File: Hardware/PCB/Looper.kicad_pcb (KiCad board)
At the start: 2 copper layers, 50 x 110.2 mm, 64 parts, among them J1 Out right, J10 Audio from Daisy, connect to 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, J13 Audio to Daisy, connect to J13, J14 Audio from Daisy, connect to 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, J15 Audio input, connect to J18, J16 Audio output, connect to J17, J17 Audio output, connect to J16, J18 Audio input, connect to J15, J2 In left, J3 Trig Loop, J4 Out left, J5 In right, J6 Eurorack_Power, J9 Audio to Daisy, connect to J13, U1 TL074, U2 TL074

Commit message: Version 1.0 of hardware ordered
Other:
- board text added: "Loop v1.0"
- board text added: "Serial"
- board text added: "by Geir & Adam"
- board text added: "https://github.com/GugeNet/Loop"
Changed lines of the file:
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@@
   (gr_rect (start 33.35 -108.5) (end 39.85 -105.3)
+    (stroke (width 0.15) (type solid)) (fill solid) (layer "B.SilkS"))
+  (gr_rect (start 31.775 -77.2) (end 41.025 -72.4)
     (stroke (width 0.15) (type solid)) (fill solid) (layer "B.SilkS"))
   (gr_rect (start 0 -119.7) (end 20 -9.6)
@@
   (gr_rect (start 0 -128.5) (end 20 0)
     (stroke (width 0.15) (type default)) (fill none) (layer "User.1"))
+  (gr_text "by Geir\n& Adam" (at 40 -80.4) (layer "B.SilkS")
+    (effects (font (size 1.5 1.5) (thickness 0.22)) (justify bottom mirror))
+  )
+  (gr_text "Loop\nv1.0" (at 40.2 -85.2) (layer "B.SilkS")
+    (effects (font (size 2 2) (thickness 0.3)) (justify bottom mirror))
+  )
+  (gr_text "https://github.com/GugeNet/Loop" (at 43.2 -119.4 90) (layer "B.SilkS")
+    (effects (font (size 1 1) (thickness 0.15)) (justify left bottom mirror))
+  )
+  (gr_text "Serial" (at 48.2 -73.6) (layer "B.SilkS")
+    (effects (font (size 1.5 1.5) (thickness 0.22)) (justify left bottom mirror))
+  )
   (segment (start 34.9 -95.5) (end 37.00828 -95.5) (width 0.25) (layer "F.Cu") (net 1))
   (segment (start 31.8 -117.58) (end 34.36 -115.02) (width 0.25) (layer "F.Cu") (net 1))
@@
         (xy 30 -120)
         (xy 50 -120)
-        (xy 50 -72.5)
-        (xy 30 -72.5)
+        (xy 50 -71.7)
+        (xy 30 -71.7)
       )
     )
@@
         (xy 30 -120)
         (xy 50 -120)
-        (xy 50 -72.5)
-        (xy 30 -72.5)
+        (xy 50 -71.7)
+        (xy 30 -71.7)
       )
     )

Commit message: Leveller 1.0b
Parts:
- moved J6 3.06 mm to (36.0, -104.4)
- moved FB1 2.48 mm to (37.2, -99.6)
- moved D1 2.45 mm to (37.1, -101.8)
- moved R22 1.88 mm to (41.0, -99.6)
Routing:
- net -12V: track 33.6 -> 30.6 mm
- net Net-(C9-Pad1): track 6.79 -> 8.73 mm
- net Net-(J18-Pin_3): track 19.2 -> 17.4 mm
- net Net-(D4-K): track 15.0 -> 13.1 mm
- net GND: track 489.2 -> 488.4 mm
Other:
- board text added: "Loop v1.0b"
- board text removed: "Loop v1.0"

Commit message: Fixed power diode polarity
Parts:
- moved FB2 16.6 mm to (35.4, -117.6)
- moved D4 11.7 mm to (40.0, -117.6), turned to 180 degrees
- moved C6 3.67 mm to (43.4, -105.3)
- moved FB1 3.35 mm to (35.1, -102.2), turned to 180 degrees
- moved C4 3.07 mm to (43.4, -112.8), turned to -90 degrees
- moved D1 2.16 mm to (36.0, -100.0), turned to 0 degrees
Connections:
- C4 pad 1: Net-(D4-K) -> +12V
- C6 pad 2: Net-(D1-A) -> -12V
- D1 pad 2: Net-(D1-A) -> -12V
- D4 pad 1: Net-(D4-K) -> +12V
- FB1 pad 1: -12V -> Net-(J6-Pin_1)
- FB2 pad 1: +12V -> Net-(J6-Pin_10)
- J6 pad 1: Net-(D1-A) -> Net-(J6-Pin_1)
- J6 pad 10: Net-(D4-K) -> Net-(J6-Pin_10)
- J6 pad 2: Net-(D1-A) -> Net-(J6-Pin_1)
- J6 pad 9: Net-(D4-K) -> Net-(J6-Pin_10)
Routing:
- net +12V: track 97.7 -> 111.9 mm
- net Net-(D4-K): track 13.1 -> 0.00 mm
- net Net-(D1-A): track 10.9 -> 0.00 mm
- net -12V: track 30.6 -> 39.8 mm
- net GND: track 488.4 -> 495.5 mm
- net Net-(J6-Pin_1): track 0.00 -> 4.70 mm
- net Net-(J6-Pin_10): track 0.00 -> 3.63 mm
- net Net-(D4-A): track 1.62 -> 2.12 mm
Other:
- board text added: "Loop v1.0c"
- board text removed: "Loop v1.0b"

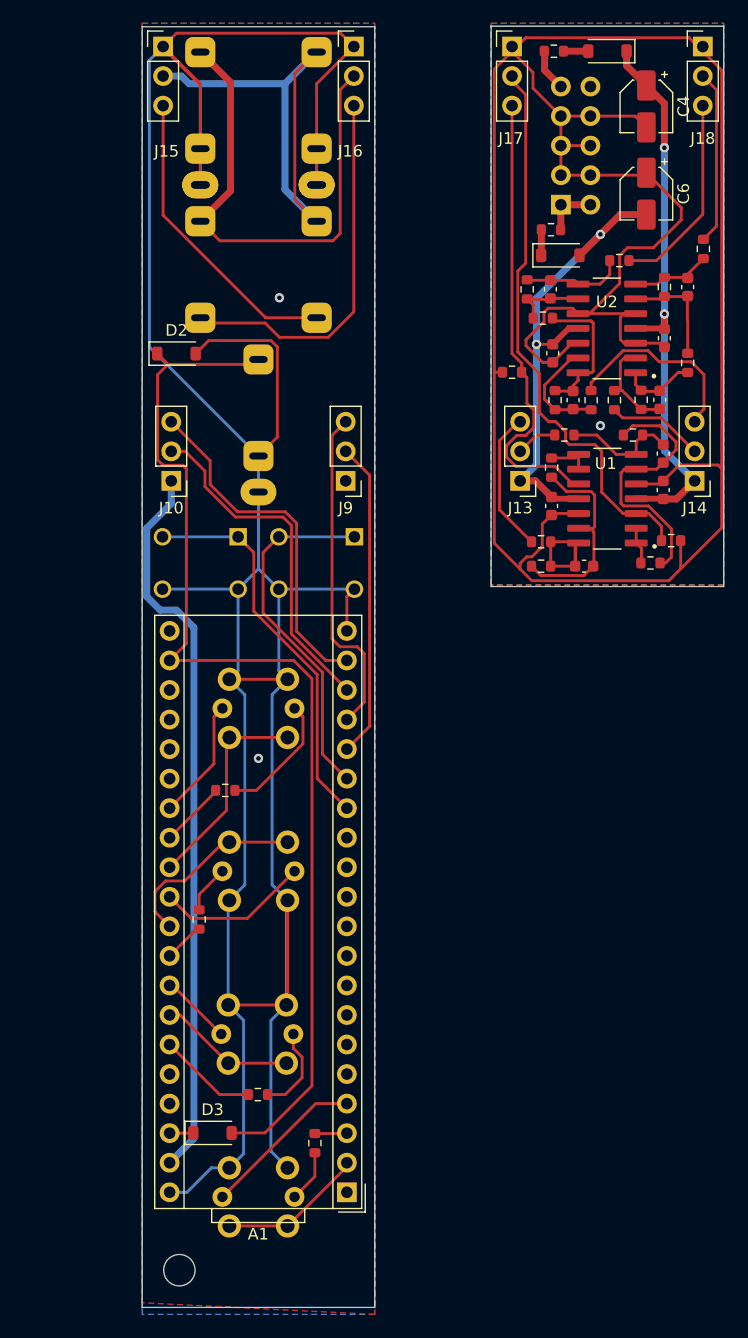
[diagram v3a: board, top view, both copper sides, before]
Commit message: new intracard connections
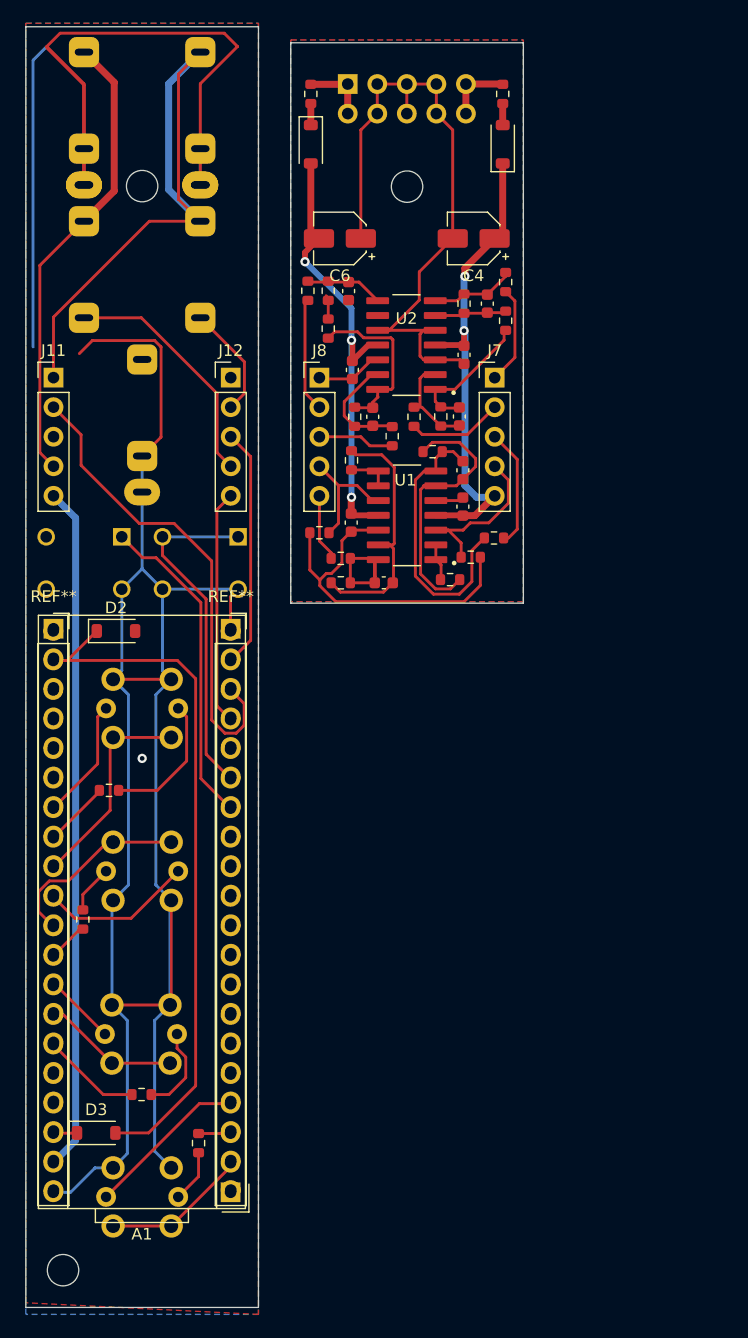
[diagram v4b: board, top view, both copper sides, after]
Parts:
- removed J10: Audio from Daisy, connect to J14, Connector_PinHeader_2.54mm:PinHeader_1x03_P2.54mm_Vertical
- removed J13, J9: Audio to Daisy, connect to J13, Connector_PinHeader_2.54mm:PinHeader_1x03_P2.54mm_Vertical
- removed J14: Audio from Daisy, connect to J10, Connector_PinHeader_2.54mm:PinHeader_1x03_P2.54mm_Vertical
- removed J15: Audio input, connect to J18, Connector_PinHeader_2.54mm:PinHeader_1x03_P2.54mm_Vertical
- removed J16: Audio output, connect to J17, Connector_PinHeader_2.54mm:PinHeader_1x03_P2.54mm_Vertical
- removed J17: Audio output, connect to J16, Connector_PinHeader_2.54mm:PinHeader_1x03_P2.54mm_Vertical
- removed J18: Audio input, connect to J15, Connector_PinHeader_2.54mm:PinHeader_1x03_P2.54mm_Vertical
- added J11: Conn_01x05, Connector_PinHeader_2.54mm:PinHeader_1x05_P2.54mm_Vertical, F.Cu at (-7.62, -89.5)
- added J12: Conn_01x05, Connector_PinHeader_2.54mm:PinHeader_1x05_P2.54mm_Vertical, F.Cu at (7.62, -89.5)
- added J7: Conn_01x05, Connector_PinHeader_2.54mm:PinHeader_1x05_P2.54mm_Vertical, F.Cu at (30.3, -89.5)
- added J8: Conn_01x05, Connector_PinHeader_2.54mm:PinHeader_1x05_P2.54mm_Vertical, F.Cu at (15.2, -89.5)
- added MOUNT1: MountingHole_2.7mm_M2.5, MountingHole:MountingHole_2.7mm_M2.5, F.Cu at (0.00, -106.0)
- added MOUNT1: MountingHole_2.7mm_M2.5, MountingHole:MountingHole_2.7mm_M2.5, F.Cu at (22.8, -106.0)
- added REF**: PinSocket_1x20_P2.54mm_Vertical, Connector_PinSocket_2.54mm:PinSocket_1x20_P2.54mm_Vertical, F.Cu at (7.62, -67.9)
- added REF**: PinSocket_1x20_P2.54mm_Vertical, Connector_PinSocket_2.54mm:PinSocket_1x20_P2.54mm_Vertical, F.Cu at (-7.62, -67.9)
- moved R22 26.9 mm to (14.2, -97.0), turned to 90 degrees
- moved C6 26.6 mm to (17.0, -101.5), turned to 180 degrees
- moved D2 24.4 mm to (-2.25, -67.8)
- moved FB1 23.7 mm to (14.5, -113.9), turned to -90 degrees
- moved D1 23.5 mm to (14.5, -109.6), turned to -90 degrees
- moved R9 21.6 mm to (15.2, -76.2)
- moved J6 21.1 mm to (17.7, -114.8), turned to -90 degrees
- moved C4 18.7 mm to (28.5, -101.5), turned to 180 degrees
- moved R20 18.5 mm to (16.0, -93.8), turned to -90 degrees
- moved R21 17.4 mm to (21.5, -84.5)
- moved C9 17.4 mm to (17.8, -97.0)
- moved C3 17.3 mm to (20.8, -71.9)
- moved C5 17.3 mm to (18.0, -77.1)
- moved C7 17.3 mm to (27.3, -86.2)
- moved R5 17.3 mm to (28.2, -74.1)
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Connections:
- A1 pad 16: Net-(A1-AUDIO_IN_L) -> DAISY_AUDIO_IN_L
- A1 pad 17: Net-(A1-AUDIO_IN_R) -> DAISY_AUDIO_IN_R
- A1 pad 18: Net-(A1-AUDIO_OUT_L) -> DAISY_AUDIO_OUT_L
- A1 pad 19: Out_R -> DAISY_AUDIO_OUT_R
- J5 pad T: Net-(J15-Pin_3) -> In Right
- R12 pad 2: Net-(J13-Pin_3) -> DAISY_AUDIO_IN_R
- R14 pad 2: Net-(J14-Pin_2) -> DAISY_AUDIO_OUT_L
- R16 pad 1: Net-(J18-Pin_2) -> In Left
- R21 pad 2: Net-(J14-Pin_3) -> DAISY_AUDIO_OUT_R
- R22 pad 1: Net-(J18-Pin_3) -> In Right
- R5 pad 1: Net-(J17-Pin_2) -> Out Left
- R8 pad 2: Net-(J13-Pin_2) -> DAISY_AUDIO_IN_L
- R9 pad 1: Net-(J17-Pin_3) -> Out Right
- U1 pad 10: Net-(J17-Pin_3) -> Out Right
- U1 pad 3: Net-(J17-Pin_2) -> Out Left
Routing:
- net GND: track 495.5 -> 354.9 mm, vias 3 -> 1
- net DAISY_AUDIO_OUT_L: track 0.00 -> 49.5 mm
- net Net-(J17-Pin_2): track 47.8 -> 0.00 mm
- net Net-(J17-Pin_3): track 39.1 -> 0.00 mm
- net Net-(A1-ADC_INP10): track 93.6 -> 61.3 mm
- net Out_R: track 30.2 -> 0.00 mm
- net Net-(A1-AUDIO_OUT_L): track 29.8 -> 0.00 mm
- net Net-(A1-AUDIO_IN_R): track 28.7 -> 0.00 mm
- net Net-(A1-AUDIO_IN_L): track 27.3 -> 0.00 mm
- net DAISY_AUDIO_OUT_R: track 0.00 -> 27.2 mm
- net Net-(J15-Pin_3): track 26.3 -> 0.00 mm
- net DAISY_AUDIO_IN_R: track 0.00 -> 26.0 mm
- net In Right: track 0.00 -> 19.5 mm
- net In Left: track 43.6 -> 62.6 mm
- net Net-(J18-Pin_3): track 17.3 -> 0.00 mm
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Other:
- board size 50 x 110.2 mm -> 42.8 x 110.1 mm

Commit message: more labels
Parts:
- removed REF** (x2): PinSocket_1x20_P2.54mm_Vertical, Connector_PinSocket_2.54mm:PinSocket_1x20_P2.54mm_Vertical
- added J9: Conn_01x20_MountingPin, Connector_PinHeader_2.54mm:PinHeader_1x20_P2.54mm_Vertical, F.Cu at (14.7, -19.6)
- moved R8 6.44 mm to (29.8, -82.2), turned to 90 degrees
- moved R20 5.73 mm to (20.3, -90.0)
- moved R9 5.52 mm to (20.3, -78.4), turned to -90 degrees
- moved C1 4.82 mm to (31.6, -75.8), turned to 180 degrees
- moved R10 4.62 mm to (22.6, -82.0)
- moved R19 4.48 mm to (22.7, -86.6), turned to 0 degrees
- moved R1 4.30 mm to (-4.32, -28.4)
- moved R17 4.18 mm to (31.8, -96.8)
- moved R6 4.13 mm to (30.6, -72.0)
- moved C10 3.60 mm to (22.7, -88.3), turned to 0 degrees
- moved C12 3.57 mm to (30.9, -93.1)
- moved C2 3.54 mm to (29.8, -78.9)
- moved C11 3.14 mm to (18.9, -93.2)
- moved U1 2.95 mm to (25.1, -75.8)
- moved R7 2.88 mm to (27.3, -81.4)
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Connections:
- R4 pad 1: Net-(A1-SDMMC1_D2) -> Net-(R4-Pad1)
- R4 pad 2: Net-(R4-Pad2) -> Net-(A1-SDMMC1_D2)
- SW4 pad 4: Net-(R4-Pad2) -> Net-(R4-Pad1)
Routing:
- net GND: track 354.9 -> 269.5 mm, vias 1 -> 0
- net Net-(A1-ADC_INP10): track 61.3 -> 92.4 mm
- net DAISY_AUDIO_IN_L: track 10.2 -> 39.7 mm
- net Net-(C2-Pad2): track 24.5 -> 6.03 mm
- net In Left: track 62.6 -> 47.4 mm
- net Net-(U2C--): track 1.68 -> 13.7 mm
- net Net-(C10-Pad1): track 14.9 -> 5.62 mm
- net DAISY_AUDIO_OUT_L: track 49.5 -> 42.1 mm
- net Net-(U1D--): track 22.5 -> 15.2 mm
- net Net-(A1-DAC1_OUT1): track 13.2 -> 20.2 mm
- net Net-(A1-USART1_TX): track 27.9 -> 33.7 mm
- net Net-(U1B--): track 24.2 -> 19.1 mm
- net Net-(R1-Pad2): track 7.64 -> 12.4 mm
- net Net-(R4-Pad1): track 0.00 -> 4.58 mm
- net Net-(R4-Pad2): track 4.52 -> 0.00 mm
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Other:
- board size 42.8 x 110.1 mm -> 45.1 x 110.1 mm

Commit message: Endret hele leveller
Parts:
- removed D2, D3: 1N5819, Diode_SMD:D_SOD-123
- added C13: 560pF, Capacitor_SMD:C_0603_1608Metric, F.Cu at (63.1, -103.0)
- added C14: 47pF, Capacitor_SMD:C_0603_1608Metric, F.Cu at (72.8, -88.9)
- added Q1: MMBT3904, Package_TO_SOT_SMD:SOT-23, F.Cu at (3.56, -87.3)
- added R23: 100K, Resistor_SMD:R_0603_1608Metric, F.Cu at (67.9, -89.2)
- added R24: 100K, Resistor_SMD:R_0603_1608Metric, F.Cu at (72.8, -90.8)
- added R25: 100K, Resistor_SMD:R_0603_1608Metric, F.Cu at (75.1, -78.5)
- added R26: 10K, Resistor_SMD:R_0603_1608Metric, F.Cu at (-4.32, -79.8)
- added R27: 1K, Resistor_SMD:R_0603_1608Metric, F.Cu at (-4.83, -66.7)
- added R28: 1M, Resistor_SMD:R_0603_1608Metric, F.Cu at (7.87, -92.5)
- C2: value 560pF -> 47pF
- R11: value 10K -> 100K
- R5: value 2M -> 10K
- R9: value 2M -> 100K
- moved R12 61.6 mm to (78.4, -78.5)
- moved R18 56.1 mm to (74.3, -93.3)
- moved C3 52.3 mm to (67.9, -94.3), turned to 180 degrees
- moved C10 52.2 mm to (74.3, -96.5), turned to 90 degrees
- moved R20 51.5 mm to (71.8, -92.7), turned to 0 degrees
- moved R19 49.6 mm to (71.8, -94.3), turned to 180 degrees
- moved C7 49.5 mm to (76.1, -103.0)
- moved R13 49.5 mm to (74.4, -103.0)
- moved R22 48.6 mm to (64.9, -92.2)
- moved C9 47.8 mm to (64.2, -78.5), turned to 90 degrees
- moved C2 46.9 mm to (76.7, -78.5)
- moved R17 46.5 mm to (78.0, -101.3)
- moved U1 45.8 mm to (70.4, -81.8)
- moved C1 45.6 mm to (76.8, -81.8)
- moved C12 45.5 mm to (76.0, -99.0)
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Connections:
- net Net-(A1-ADC1_INP4) renamed SWITCH_1_RED
- net Net-(A1-ADC_INP11) renamed SWITCH_1_GREEN
- net Net-(A1-DAC1_OUT1) renamed SWITCH_2_RED
- net Net-(A1-DAC1_OUT2) renamed SWITCH_1_GPIO
- net Net-(A1-SAI2_FS_B) renamed SWITCH_3_GPIO
- net Net-(A1-SAI2_MCLK_B) renamed SWITCH_2_GPIO
- net Net-(A1-SAI2_SD_A) renamed SWITCH_3_GREEN
- net Net-(A1-SDMMC1_D1) renamed SWITCH_4_GREEN
- net Net-(A1-SDMMC1_D3) renamed SWITCH_4_GPIO
- net Net-(A1-USART1_RX) renamed CLEAR_GPIO
- A1 pad 22: Net-(A1-ADC_INP10) -> TRIG_GPIO
- A1 pad 23: unconnected-(A1-ADC_INP15-Pad23) -> RECORD_GPIO
- A1 pad 3: Net-(A1-SDMMC1_D2) -> SWITCH_4_RED
- A1 pad 32: Net-(A1-SAI2_SD_B) -> SWITCH_2_GREEN
- A1 pad 35: Net-(A1-SAI2_SCK_B) -> SWITCH_3_RED
- C10 pad 2: Net-(U2D--) -> Net-(U2A--)
- C2 pad 1: Net-(U1B--) -> Net-(C2-Pad1)
- C2 pad 2: Net-(C2-Pad2) -> Net-(U1A--)
- C3 pad 1: Net-(U1D--) -> Net-(U2D--)
- C7 pad 1: Net-(U2A--) -> Net-(U2B--)
- C8 pad 1: Net-(C8-Pad1) -> Net-(U1C--)
- C8 pad 2: Net-(U2B--) -> Net-(C8-Pad2)
- C9 pad 2: Net-(U2C--) -> Net-(U1D--)
- J1 pad TN: Out Left -> GND
- J11 pad 1: In Left -> +12V
- J11 pad 2: DAISY_AUDIO_OUT_L -> In Left
- J11 pad 3: DAISY_AUDIO_IN_L -> In Right
- J11 pad 5: +12V -> Out Right
- J12 pad 2: In Right -> DAISY_AUDIO_IN_L
- J12 pad 3: DAISY_AUDIO_OUT_R -> DAISY_AUDIO_IN_R
- J12 pad 4: Out Right -> DAISY_AUDIO_OUT_L
- J12 pad 5: DAISY_AUDIO_IN_R -> DAISY_AUDIO_OUT_R
- J3 pad T: Net-(A1-ADC_INP10) -> Net-(J3-PadT)
- J5 pad TN: In Left -> GND
- J7 pad 1: In Left -> +12V
- J7 pad 2: DAISY_AUDIO_OUT_L -> In Left
- J7 pad 3: DAISY_AUDIO_IN_L -> In Right
- J7 pad 5: +12V -> Out Right
- J8 pad 2: In Right -> DAISY_AUDIO_IN_L
- J8 pad 3: DAISY_AUDIO_OUT_R -> DAISY_AUDIO_IN_R
- J8 pad 4: Out Right -> DAISY_AUDIO_OUT_L
- J8 pad 5: DAISY_AUDIO_IN_R -> DAISY_AUDIO_OUT_R
- J9 pad 3: Net-(A1-SDMMC1_D2) -> SWITCH_4_RED
- R1 pad 1: Net-(A1-SAI2_SCK_B) -> Net-(R1-Pad1)
- R1 pad 2: Net-(R1-Pad2) -> SWITCH_3_RED
- R10 pad 1: Net-(U1C--) -> Net-(C9-Pad1)
- R10 pad 2: Net-(U1D--) -> Net-(U1A--)
- R11 pad 1: Net-(U1D--) -> Net-(Q1-B)
- R11 pad 2: Net-(C3-Pad2) -> Net-(J3-PadT)
- R12 pad 1: Net-(C3-Pad2) -> Net-(C2-Pad1)
- R12 pad 2: DAISY_AUDIO_IN_R -> Out Right
- R13 pad 1: Net-(U2A--) -> Net-(U2B--)
- R14 pad 1: Net-(U2A--) -> Net-(C13-Pad2)
- R14 pad 2: DAISY_AUDIO_OUT_L -> Net-(U2C--)
- R15 pad 1: Net-(U2B--) -> Net-(U2C--)
- R16 pad 1: In Left -> DAISY_AUDIO_IN_L
- R16 pad 2: Net-(C8-Pad1) -> Net-(C13-Pad2)
- R17 pad 1: Net-(C8-Pad1) -> Net-(U2B--)
- R17 pad 2: Net-(U2B--) -> In Left
- R18 pad 1: Net-(C9-Pad1) -> Net-(U2A--)
- R18 pad 2: Net-(U2C--) -> In Right
- R19 pad 2: Net-(U2D--) -> Net-(U2A--)
- R2 pad 1: Net-(R2-Pad1) -> SWITCH_2_GREEN
- R2 pad 2: Net-(A1-SAI2_SD_B) -> Net-(R2-Pad2)
- R20 pad 1: Net-(U2C--) -> Net-(U2D--)
- R21 pad 1: Net-(U2D--) -> Net-(C3-Pad2)
- R21 pad 2: DAISY_AUDIO_OUT_R -> Net-(U2D--)
- R22 pad 1: In Right -> DAISY_AUDIO_IN_R
- R22 pad 2: Net-(C9-Pad1) -> Net-(C3-Pad2)
- R4 pad 1: Net-(R4-Pad1) -> SWITCH_4_RED
- R4 pad 2: Net-(A1-SDMMC1_D2) -> Net-(R4-Pad2)
- R5 pad 1: Out Left -> Net-(U1D--)
- R5 pad 2: GND -> DAISY_AUDIO_OUT_R
- R6 pad 1: Net-(U1A--) -> Net-(C8-Pad2)
- R7 pad 1: Net-(U1B--) -> DAISY_AUDIO_OUT_L
- R7 pad 2: Net-(C2-Pad2) -> Net-(U1C--)
- R8 pad 1: Net-(C2-Pad2) -> Out Left
- R8 pad 2: DAISY_AUDIO_IN_L -> Net-(C14-Pad2)
- R9 pad 1: Out Right -> Net-(U1D--)
- R9 pad 2: GND -> Net-(C9-Pad1)
- S2 pad 1: Net-(A1-USART1_TX) -> RECORD_GPIO
- SW2 pad 3: Net-(R2-Pad1) -> Net-(R2-Pad2)
- SW3 pad 4: Net-(R1-Pad2) -> Net-(R1-Pad1)
- SW4 pad 4: Net-(R4-Pad1) -> Net-(R4-Pad2)
- U1 pad 1: Net-(U1A--) -> Net-(C2-Pad1)
- U1 pad 10: Out Right -> GND
- U1 pad 14: Net-(C3-Pad2) -> Net-(C9-Pad1)
- U1 pad 3: Out Left -> GND
- U1 pad 7: Net-(C2-Pad2) -> Net-(C14-Pad2)
- U1 pad 8: Net-(U1C--) -> Net-(C8-Pad2)
- U2 pad 1: Net-(C7-Pad2) -> Net-(C10-Pad1)
- U2 pad 14: Net-(C10-Pad1) -> Net-(C3-Pad2)
- U2 pad 7: Net-(C8-Pad1) -> Net-(C7-Pad2)
- U2 pad 8: Net-(C9-Pad1) -> Net-(C13-Pad2)
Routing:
- net Net-(A1-ADC_INP10): track 92.4 -> 0.00 mm
- net +3.3V: track 2.05 -> 55.8 mm, vias 0 -> 1
- net GND: track 269.5 -> 322.8 mm
- net Net-(A1-USART1_TX): track 33.7 -> 0.00 mm
- net RECORD_GPIO: track 0.00 -> 31.1 mm
- net Net-(Q1-C): track 0.00 -> 28.1 mm
- net DAISY_AUDIO_OUT_L: track 42.1 -> 24.6 mm
- net +12V: track 104.4 -> 119.0 mm
- net Net-(U1A--): track 3.52 -> 17.0 mm
- net Net-(R1-Pad2): track 12.4 -> 0.00 mm
- net Net-(C8-Pad2): track 0.00 -> 11.6 mm
- net Out Left: track 54.7 -> 44.1 mm
- net Net-(U1B--): track 19.1 -> 8.98 mm
- net Net-(U1D--): track 15.2 -> 5.50 mm
- net Net-(R1-Pad1): track 0.00 -> 9.61 mm
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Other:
- board size 45.1 x 110.1 mm -> 89.7 x 114.6 mm

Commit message: HW 1.0c
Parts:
- removed J9: Conn_01x20_MountingPin, Connector_PinHeader_2.54mm:PinHeader_1x20_P2.54mm_Vertical
- removed R28: 1M, Resistor_SMD:R_0603_1608Metric
- added R29: 100K, Resistor_SMD:R_0603_1608Metric, F.Cu at (86.9, 85.3)
- moved C1 203.1 mm to (144.7, 109.7)
- moved C10 203.1 mm to (142.1, 94.9)
- moved C14 203.1 mm to (140.6, 102.5)
- moved C2 203.1 mm to (144.5, 113.0)
- moved C3 203.1 mm to (135.7, 97.1)
- moved C5 203.1 mm to (130.7, 109.7)
- moved C8 203.1 mm to (135.7, 104.1)
- moved C9 203.1 mm to (132.0, 113.0)
- moved D1 203.1 mm to (129.2, 76.0)
- moved D4 203.1 mm to (145.7, 76.0)
- moved FB1 203.1 mm to (129.2, 71.7)
- moved FB2 203.1 mm to (145.7, 71.7)
- moved R10 203.1 mm to (129.6, 113.3)
- moved R12 203.1 mm to (146.2, 113.0)
- moved R16 203.1 mm to (129.3, 88.5)
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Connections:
- A1 pad 14: Net-(A1-USART1_TX) -> unconnected-(A1-USART1_TX-Pad14)
- A1 pad 22: TRIG_GPIO -> RECORD_GPIO
- A1 pad 23: RECORD_GPIO -> TRIG_GPIO
- A1 pad 24: unconnected-(A1-ADC_INP5-Pad24) -> SWITCH_1_GREEN
- A1 pad 25: unconnected-(A1-ADC_INP7-Pad25) -> SWITCH_1_RED
- A1 pad 26: unconnected-(A1-ADC_INP3-Pad26) -> SWITCH_1_GPIO
- A1 pad 27: SWITCH_1_GREEN -> SWITCH_2_GPIO
- A1 pad 28: SWITCH_1_RED -> SWITCH_2_RED
- A1 pad 29: SWITCH_1_GPIO -> SWITCH_2_GREEN
- A1 pad 30: SWITCH_2_RED -> unconnected-(A1-DAC1_OUT1-Pad30)
- A1 pad 31: SWITCH_2_GPIO -> unconnected-(A1-SAI2_MCLK_B-Pad31)
- A1 pad 32: SWITCH_2_GREEN -> unconnected-(A1-SAI2_SD_B-Pad32)
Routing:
- net GND: track 322.8 -> 365.9 mm, vias 0 -> 1
- net SWITCH_2_RED: track 20.0 -> 11.9 mm
- net SWITCH_1_GREEN: track 11.5 -> 4.94 mm
- net RECORD_GPIO: track 31.1 -> 26.0 mm
- net SWITCH_1_GPIO: track 17.9 -> 12.8 mm
- net Net-(R3-Pad1): track 15.5 -> 10.8 mm
- net TRIG_GPIO: track 2.59 -> 6.43 mm
- net SWITCH_2_GPIO: track 14.3 -> 11.3 mm
- net Net-(Q1-C): track 28.1 -> 26.5 mm
- net SWITCH_1_RED: track 4.10 -> 2.55 mm
- net Net-(R2-Pad2): track 5.85 -> 4.36 mm
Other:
- board size 89.7 x 114.6 mm -> 78.5 x 110.1 mm
